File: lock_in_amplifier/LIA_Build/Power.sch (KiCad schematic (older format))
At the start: 60 parts, among them J1 vref-in, J19 +3V3 OUT, J2 vref, J3 V-IN, J4 GND, J46 -5V OUT, J47 +5V OUT, J5 V+IN, J6 +5V, J7 +3V3, J8 -5V, Q1 DMN640L, Q2 DMN640L, U1 LM833, U2 lm7805, U3 LM7833, U4 lm7905

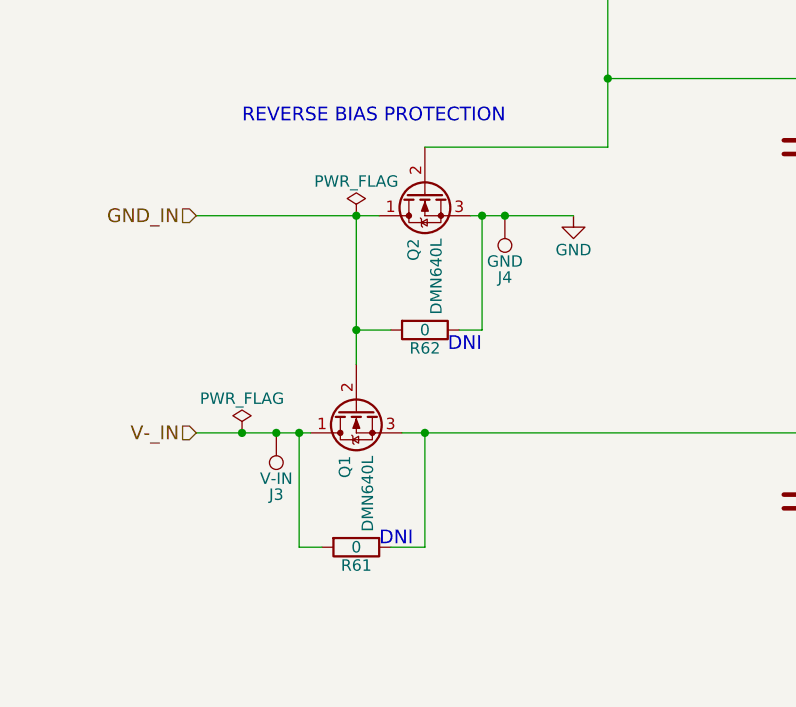
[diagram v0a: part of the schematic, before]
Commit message: initial lna and power floorplan finished.
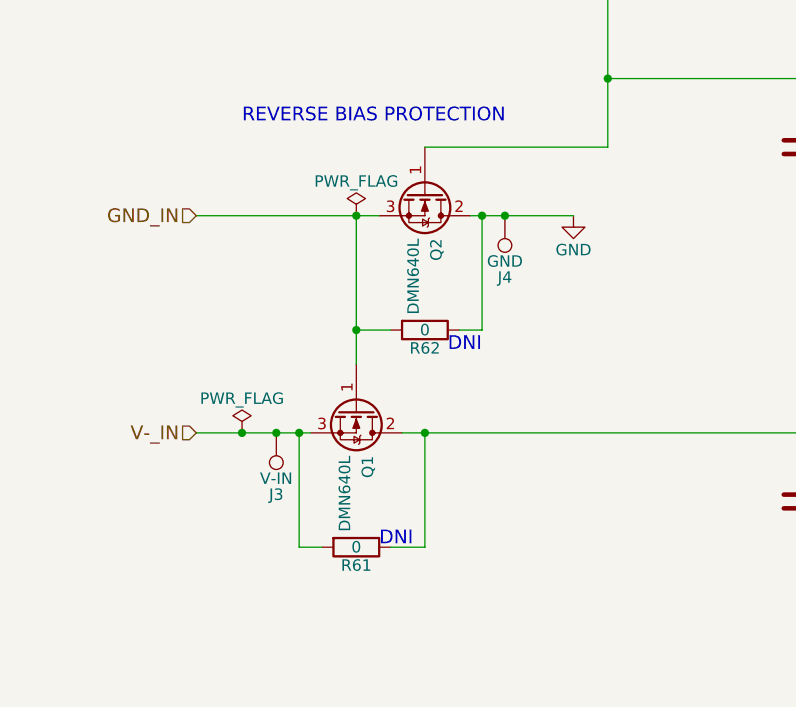
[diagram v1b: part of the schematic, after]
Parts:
- removed Q1, Q2: DMN640L, TO_SOT_Packages_SMD:SOT-23, symbol Q_NMOS_DGS
- added Q1, Q2: DMN640L, symbol Q_NMOS_GDS
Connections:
- net GND: now also Q2.2 (D)
- net GND_IN: now also Q1.1 (G), Q2.3 (S)
- net V+_IN: now also Q2.1 (G)
- net V-_IN: now also Q1.3 (S)
- net at C10.1, L4.2, R61.1: now also Q1.2 (D)
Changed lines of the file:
@@
 	1    0    0    -1
-$EndComp
-$Comp
-L Q_NMOS_DGS Q2
-U 1 1 5A1CC551
-P 3650 3100
-F 0 "Q2" H 3850 3150 50  0000 L CNN
-F 1 "DMN640L" H 3850 3050 50  0000 L CNN
-F 2 "TO_SOT_Packages_SMD:SOT-23" H 3850 3200 50  0001 C CNN
-F 3 "" H 3650 3100 50  0001 C CNN
-	1    3650 3100
-	0    -1   1    0
-$EndComp
-$Comp
-L Q_NMOS_DGS Q1
-U 1 1 5A1CC5CE
-P 3350 4050
-F 0 "Q1" H 3550 4100 50  0000 L CNN
-F 1 "DMN640L" H 3550 4000 50  0000 L CNN
-F 2 "TO_SOT_Packages_SMD:SOT-23" H 3550 4150 50  0001 C CNN
-F 3 "" H 3350 4050 50  0001 C CNN
-	1    3350 4050
-	0    -1   1    0
 $EndComp
 Connection ~ 7300 1350
@@
 	1    0    0    -1
 $EndComp
+$Comp
+L Q_NMOS_GDS Q2
+U 1 1 5A344295
+P 3650 3100
+F 0 "Q2" H 3850 3150 50  0000 L CNN
+F 1 "DMN640L" H 3850 3050 50  0000 L CNN
+F 2 "" H 3850 3200 50  0001 C CNN
+F 3 "" H 3650 3100 50  0001 C CNN
+	1    3650 3100
+	0    1    1    0
+$EndComp
+$Comp
+L Q_NMOS_GDS Q1
+U 1 1 5A344D49
+P 3350 4050
+F 0 "Q1" H 3550 4100 50  0000 L CNN
+F 1 "DMN640L" H 3550 4000 50  0000 L CNN
+F 2 "" H 3550 4150 50  0001 C CNN
+F 3 "" H 3350 4050 50  0001 C CNN
+	1    3350 4050
+	0    1    1    0
+$EndComp
 $EndSCHEMATC

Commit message: adressing comments - fets
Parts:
- removed Q1, Q2: DMN640L, symbol Q_NMOS_GDS
- added D14, D15: BAT54S, TO_SOT_Packages_SMD:SOT-23, symbol D_Schottky_x2_Serial_AKC
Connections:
- net GND_IN is gone; now on net V+_IN: R62.2
- net GND: no longer R62.1
- net V+_IN: now also D15.3 (common); no longer C8.1, C9.1, J5.1, L2.1, L3.2
- net V-_IN: now also D14.2 (K)
- net at C10.1, L4.2, R61.1: now also D14.3 (common)
- new net: C8.1, C9.1, D15.2 (K), J5.1, L2.1, L3.2, R62.1
- no-connect marks 0 -> 2
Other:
- note added: "PI FILTERS - DNI / 0 OHM\nINCLUDE IF NECCESARY"
- moved on the sheet: R62
